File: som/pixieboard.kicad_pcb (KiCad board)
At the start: 8 copper layers, 50 x 50 mm, 11 parts, among them U1 XC7A200T-3FBG484E, U2 AS4C256M16D3, U3 AS4C256M16D3

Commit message: lmfao l
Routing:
- net /DDR3/DDR_D23: track 34.2 -> 0.57 mm, vias 3 -> 1
- net /DDR3/DDR_D17: track 28.9 -> 0.57 mm, vias 3 -> 1
- net /DDR3/DDR_D19: track 28.4 -> 0.57 mm, vias 2 -> 1
- net /DDR3/DDR_DM2: track 28.1 -> 0.57 mm, vias 3 -> 1
- net /DDR3/DDR_D22: track 27.9 -> 0.57 mm, vias 4 -> 1
- net /DDR3/DDR_D21: track 27.3 -> 0.57 mm, vias 3 -> 1
- net /DDR3/DDR_D30: track 26.2 -> 0.57 mm, vias 3 -> 1
- net /DDR3/DDR_D24: track 25.0 -> 0.57 mm, vias 3 -> 1
- net /DDR3/DDR_D16: track 23.8 -> 0.57 mm, vias 3 -> 1
- net /DDR3/DDR_D20: track 23.6 -> 0.57 mm, vias 4 -> 1
- net /DDR3/DDR_DQS3+: track 23.2 -> 0.57 mm, vias 3 -> 1
- net /DDR3/DDR_DQS2-: track 22.8 -> 0.57 mm, vias 2 -> 1
- net /DDR3/DDR_DQS3-: track 22.4 -> 0.57 mm, vias 3 -> 1
- net /DDR3/DDR_D18: track 22.2 -> 0.57 mm, vias 4 -> 1
- net /DDR3/DDR_DM3: track 21.8 -> 0.57 mm, vias 3 -> 1
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
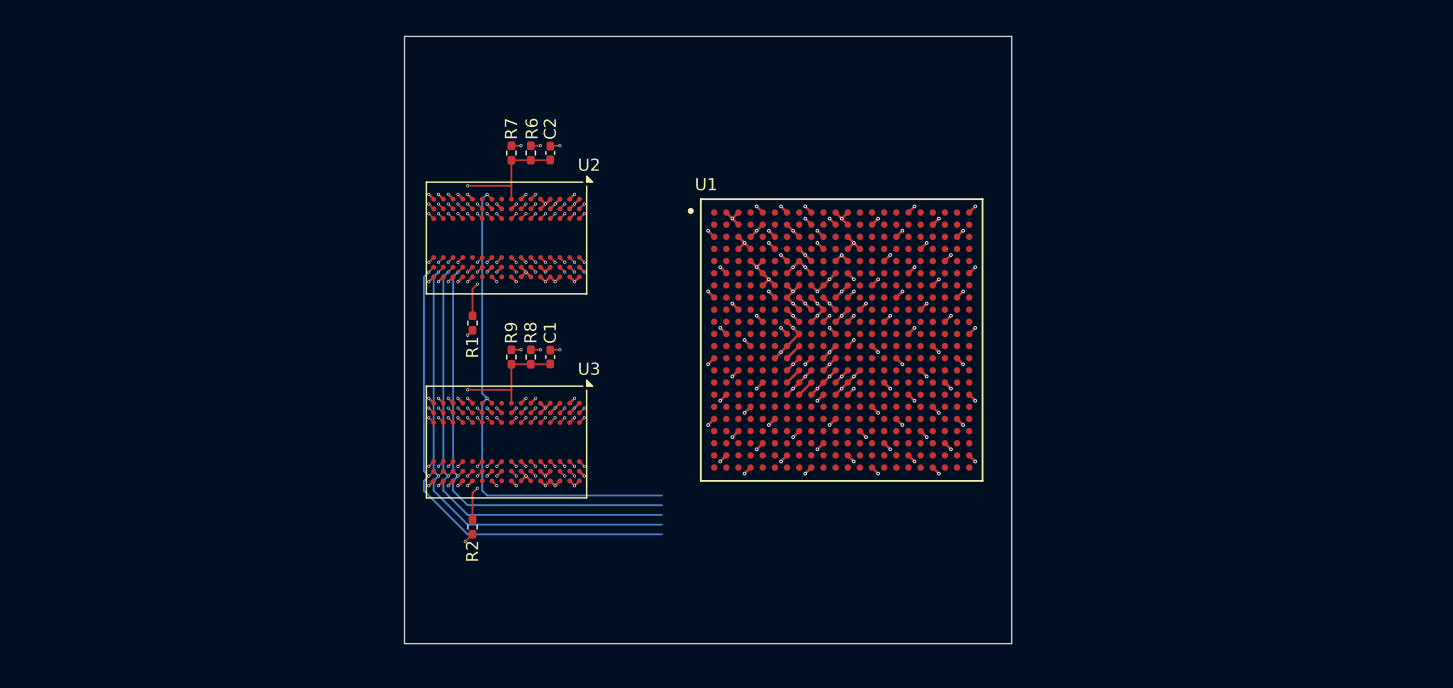
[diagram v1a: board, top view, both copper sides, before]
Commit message: Completed DDR3L routing
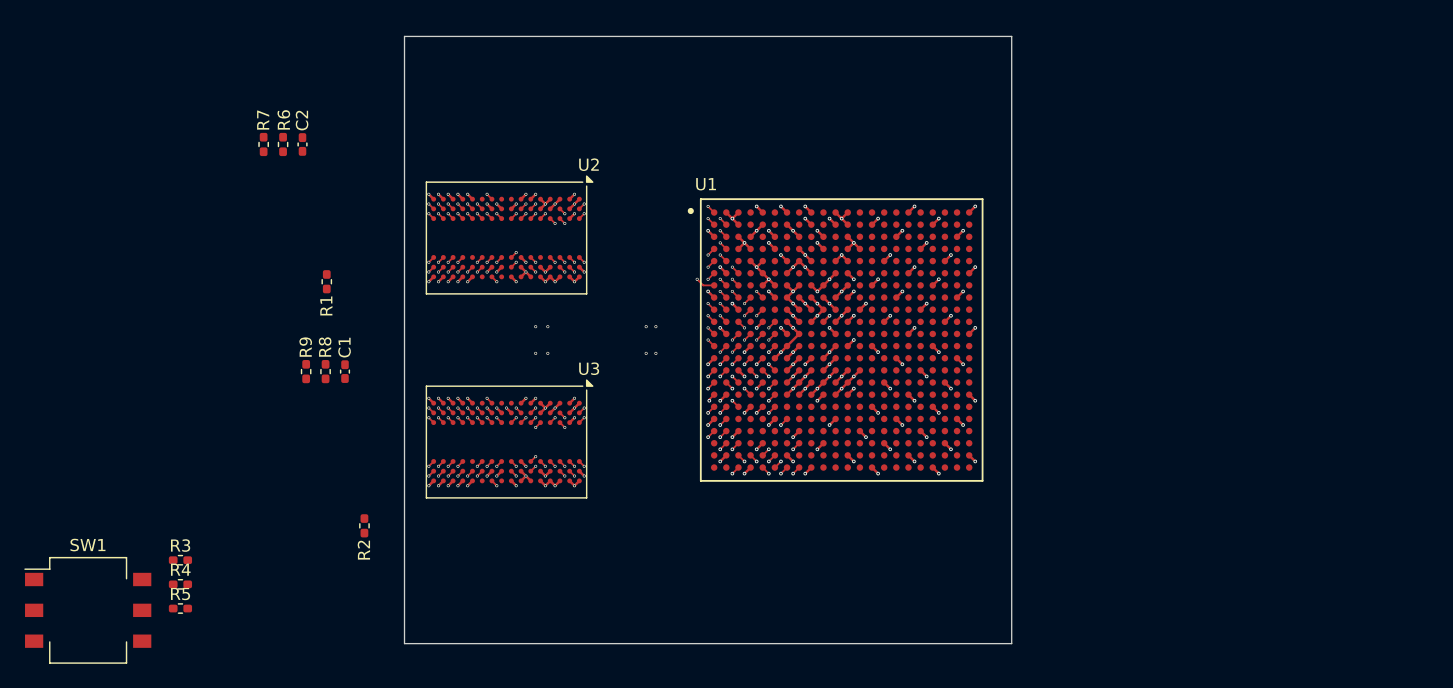
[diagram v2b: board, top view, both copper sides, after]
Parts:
- added R3: 10K, Resistor_SMD:R_0402_1005Metric_Pad0.72x0.64mm_HandSolder, F.Cu at (-54.5, 18.1)
- added R4: 10K, Resistor_SMD:R_0402_1005Metric_Pad0.72x0.64mm_HandSolder, F.Cu at (-54.5, 20.1)
- added R5: 10K, Resistor_SMD:R_0402_1005Metric_Pad0.72x0.64mm_HandSolder, F.Cu at (-54.5, 22.1)
- added SW1: SW_DIP_x03, Button_Switch_SMD:SW_DIP_SPSTx03_Slide_Omron_A6S-310x_W8.9mm_P2.54mm, F.Cu at (-62.0, 22.3)
- moved R7 20.4 mm to (-47.6, -16.1)
- moved C2 20.4 mm to (-44.4, -16.1)
- moved R6 20.4 mm to (-46.0, -16.1)
- moved R9 16.9 mm to (-44.1, 2.60)
- moved C1 16.9 mm to (-40.9, 2.60)
- moved R8 16.9 mm to (-42.5, 2.60)
- moved R1 12.5 mm to (-42.4, -4.80)
- moved R2 8.90 mm to (-39.3, 15.3)
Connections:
- U1 pad A1: /DDR3/DDR_D1 -> /DDR3/DDR_D4
- U1 pad AA1: /DDR3/DDR_A8 -> unconnected-(U1E-IO_L7P_T1_34-PadAA1)
- U1 pad AA3: /DDR3/DDR_A13 -> /DDR3/DDR_BA2
- U1 pad AA4: /DDR3/DDR_BA2 -> /DDR3/DDR_A5
- U1 pad AA5: /DDR3/DDR_A14 -> /DDR3/DDR_A0
- U1 pad AA6: unconnected-(U1E-IO_L18N_T2_34-PadAA6) -> /DDR3/DDR_A7
- U1 pad AA8: /DDR3/~{DDR_RST} -> unconnected-(U1E-IO_L22P_T3_34-PadAA8)
- U1 pad AB1: /DDR3/DDR_A9 -> unconnected-(U1E-IO_L7N_T1_34-PadAB1)
- U1 pad AB2: /DDR3/DDR_A11 -> unconnected-(U1E-IO_L8N_T1_34-PadAB2)
- U1 pad AB3: /DDR3/DDR_A10 -> /DDR3/DDR_A3
- U1 pad AB5: /DDR3/DDR_BA0 -> /DDR3/DDR_A2
- U1 pad AB6: unconnected-(U1E-IO_L20N_T3_34-PadAB6) -> /DDR3/~{DDR_RST}
- U1 pad AB7: unconnected-(U1E-IO_L20P_T3_34-PadAB7) -> /DDR3/DDR_A9
- U1 pad AB8: /DDR3/~{DDR_CS} -> /DDR3/DDR_A13
- U1 pad B1: /DDR3/DDR_D0 -> /DDR3/DDR_D6
- U1 pad B2: /DDR3/DDR_D3 -> /DDR3/DDR_D2
- U1 pad C2: /DDR3/DDR_D2 -> /DDR3/DDR_D0
- U1 pad D2: /DDR3/DDR_D5 -> /DDR3/DDR_D7
- U1 pad E2: /DDR3/DDR_D4 -> /DDR3/DDR_D5
- U1 pad F1: /DDR3/DDR_D7 -> /DDR3/DDR_D3
- U1 pad F3: /DDR3/DDR_DM0 -> /DDR3/DDR_D1
- U1 pad G1: /DDR3/DDR_D6 -> /DDR3/DDR_DM0
- U1 pad G2: /DDR3/DDR_D11 -> /DDR3/DDR_D8
- U1 pad H3: /DDR3/DDR_D12 -> /DDR3/DDR_D15
- U1 pad H4: /DDR3/DDR_DM1 -> /DDR3/DDR_D11
- U1 pad H5: /DDR3/DDR_D15 -> /DDR3/DDR_DM1
- U1 pad J1: /DDR3/DDR_D9 -> /DDR3/DDR_D12
- U1 pad J4: /DDR3/DDR_D17 -> /DDR3/DDR_D22
- U1 pad J5: /DDR3/DDR_D14 -> /DDR3/DDR_D9
- U1 pad J6: /DDR3/DDR_D23 -> unconnected-(U1F-IO_L17N_T2_35-PadJ6)
- U1 pad K1: /DDR3/DDR_D8 -> /DDR3/DDR_D14
- U1 pad K3: /DDR3/DDR_D19 -> /DDR3/DDR_D20
- U1 pad K4: /DDR3/DDR_D16 -> unconnected-(U1F-IO_L13P_T2_MRCC_35-PadK4)
- U1 pad K6: /DDR3/DDR_D22 -> /DDR3/DDR_D18
- U1 pad L3: /DDR3/DDR_D18 -> /DDR3/DDR_D21
- U1 pad L4: unconnected-(U1F-IO_L18N_T2_35-PadL4) -> /DDR3/DDR_D17
- U1 pad L5: /DDR3/DDR_DM2 -> /DDR3/DDR_D19
- U1 pad L6: unconnected-(U1F-IO_25_35-PadL6) -> /DDR3/DDR_D16
- U1 pad M2: /DDR3/DDR_D21 -> /DDR3/DDR_DM2
- U1 pad M3: /DDR3/DDR_D20 -> /DDR3/DDR_D23
- U1 pad M5: /DDR3/DDR_D31 -> unconnected-(U1F-IO_L23N_T3_35-PadM5)
- U1 pad M6: /DDR3/DDR_D30 -> /DDR3/DDR_D25
- U1 pad N2: /DDR3/DDR_D29 -> /DDR3/DDR_D24
- U1 pad N3: /DDR3/DDR_D25 -> /DDR3/DDR_D29
- U1 pad N4: /DDR3/DDR_D24 -> /DDR3/DDR_D31
- U1 pad N5: unconnected-(U1F-IO_L24N_T3_35-PadN5) -> /DDR3/DDR_D27
- U1 pad P1: /DDR3/DDR_D27 -> /DDR3/DDR_D28
- U1 pad P2: /DDR3/DDR_D28 -> /DDR3/DDR_D26
- U1 pad R1: /DDR3/DDR_D26 -> /DDR3/DDR_D30
- U1 pad R2: /DDR3/DDR_A5 -> /DDR3/DDR_CLK-
- U1 pad R3: /DDR3/DDR_A4 -> /DDR3/DDR_CLK+
- U1 pad R6: unconnected-(U1E-IO_L17P_T2_34-PadR6) -> /DDR3/DDR_A12
- U1 pad T1: /DDR3/DDR_A0 -> /DDR3/DDR_CLK_E
- U1 pad T4: unconnected-(U1E-IO_L13N_T2_MRCC_34-PadT4) -> /DDR3/DDR_A10
- U1 pad T6: unconnected-(U1E-IO_L17N_T2_34-PadT6) -> /DDR3/DDR_A1
- U1 pad U1: /DDR3/DDR_A1 -> /DDR3/DDR_ODT
- U1 pad U2: /DDR3/DDR_A2 -> /DDR3/DDR_BA1
- U1 pad U3: unconnected-(U1E-IO_L6P_T0_34-PadU3) -> /DDR3/DDR_A4
- U1 pad U5: unconnected-(U1E-IO_L14N_T2_SRCC_34-PadU5) -> /DDR3/DDR_A6
- U1 pad U6: unconnected-(U1E-IO_L16P_T2_34-PadU6) -> /DDR3/DDR_A8
- U1 pad V2: /DDR3/DDR_A3 -> /DDR3/~{DDR_CS}
- U1 pad V7: /DDR3/DDR_CLK_E -> /DDR3/DDR_A11
- U1 pad W1: unconnected-(U1E-IO_L5P_T0_34-PadW1) -> /DDR3/~{DDR_RAS}
- U1 pad W2: /DDR3/DDR_A6 -> /DDR3/DDR_BA0
- U1 pad W5: /DDR3/DDR_CLK- -> unconnected-(U1E-IO_L15N_T2_DQS_34-PadW5)
- U1 pad W6: /DDR3/DDR_CLK+ -> unconnected-(U1E-IO_L15P_T2_DQS_34-PadW6)
- U1 pad W9: /DDR3/~{DDR_WE} -> unconnected-(U1E-IO_L24P_T3_34-PadW9)
- U1 pad Y2: /DDR3/DDR_A7 -> /DDR3/~{DDR_CAS}
- U1 pad Y3: /DDR3/DDR_A12 -> /DDR3/~{DDR_WE}
- U1 pad Y4: /DDR3/DDR_BA1 -> unconnected-(U1E-IO_L11P_T1_SRCC_34-PadY4)
- U1 pad Y7: /DDR3/~{DDR_CAS} -> unconnected-(U1E-IO_L23N_T3_34-PadY7)
- U1 pad Y8: /DDR3/~{DDR_RAS} -> /DDR3/DDR_A14
- U1 pad Y9: /DDR3/DDR_ODT -> unconnected-(U1E-IO_L24N_T3_34-PadY9)
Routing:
- net /DDR3/DDR_DQS2+: track 0.57 -> 31.6 mm, vias 1 -> 2
- net /DDR3/DDR_DM2: track 0.57 -> 31.6 mm, vias 1 -> 2
- net /DDR3/DDR_DQS2-: track 0.57 -> 31.6 mm, vias 1 -> 2
- net /DDR3/DDR_D23: track 0.57 -> 30.7 mm, vias 1 -> 2
- net /DDR3/DDR_D22: track 0.57 -> 30.7 mm, vias 1 -> 2
- net /DDR3/DDR_D21: track 0.57 -> 30.1 mm, vias 1 -> 2
- net /DDR3/DDR_D20: track 0.57 -> 30.1 mm, vias 1 -> 2
- net /DDR3/DDR_CLK_E: track 32.2 -> 61.6 mm, vias 2 -> 3
- net /DDR3/DDR_D17: track 0.57 -> 29.8 mm, vias 1 -> 2
- net /DDR3/DDR_D18: track 0.57 -> 29.8 mm, vias 1 -> 2
- net /DDR3/DDR_D16: track 0.57 -> 29.2 mm, vias 1 -> 2
- net /DDR3/DDR_D19: track 0.57 -> 29.1 mm, vias 1 -> 2
- net /DDR3/DDR_CLK+: track 34.9 -> 61.5 mm, vias 2 -> 3
- net /DDR3/DDR_DM1: track 0.57 -> 26.6 mm, vias 1 -> 2
- net /DDR3/DDR_DQS1+: track 0.57 -> 26.5 mm, vias 1 -> 2
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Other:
- board text added: "T0"
- board text added: "T1"
- board text added: "T2"
- board text added: "T3"

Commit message: Mezz Power Tweak Ok
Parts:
- added C10: 100nF, Capacitor_SMD:C_0402_1005Metric_Pad0.74x0.62mm_HandSolder, B.Cu at (0.50, 2.50)
- added C11: 100nF, Capacitor_SMD:C_0402_1005Metric_Pad0.74x0.62mm_HandSolder, B.Cu at (0.50, -2.50)
- added C12: 100nF, Capacitor_SMD:C_0402_1005Metric_Pad0.74x0.62mm_HandSolder, B.Cu at (-9.50, -2.00)
- added C13: 100nF, Capacitor_SMD:C_0402_1005Metric_Pad0.74x0.62mm_HandSolder, B.Cu at (-10.0, -9.50)
- added C14: 100nF, Capacitor_SMD:C_0402_1005Metric_Pad0.74x0.62mm_HandSolder, B.Cu at (-9.00, -5.50)
- added C15: 100nF, Capacitor_SMD:C_0402_1005Metric_Pad0.74x0.62mm_HandSolder, B.Cu at (-7.00, 6.50)
- added C16: 100nF, Capacitor_SMD:C_0402_1005Metric_Pad0.74x0.62mm_HandSolder, B.Cu at (-7.50, 3.50)
- added C17: 100nF, Capacitor_SMD:C_0402_1005Metric_Pad0.74x0.62mm_HandSolder, B.Cu at (-7.50, 10.0)
- added C18: 100nF, Capacitor_SMD:C_0402_1005Metric_Pad0.74x0.62mm_HandSolder, B.Cu at (7.00, -10.5)
- added C19: 100nF, Capacitor_SMD:C_0402_1005Metric_Pad0.74x0.62mm_HandSolder, B.Cu at (5.00, -6.50)
- added C20: 100nF, Capacitor_SMD:C_0402_1005Metric_Pad0.74x0.62mm_HandSolder, B.Cu at (10.0, -6.50)
- added C21: 100nF, Capacitor_SMD:C_0402_1005Metric_Pad0.74x0.62mm_HandSolder, B.Cu at (8.00, -2.50)
- added C22: 100nF, Capacitor_SMD:C_0402_1005Metric_Pad0.74x0.62mm_HandSolder, B.Cu at (2.50, -4.00)
- added C23: 100nF, Capacitor_SMD:C_0402_1005Metric_Pad0.74x0.62mm_HandSolder, B.Cu at (9.00, 1.44)
- added C24: 100nF, Capacitor_SMD:C_0402_1005Metric_Pad0.74x0.62mm_HandSolder, B.Cu at (8.00, 8.50)
- added C25: 100nF, Capacitor_SMD:C_0402_1005Metric_Pad0.74x0.62mm_HandSolder, B.Cu at (8.00, 3.50)
- added C26: 100nF, Capacitor_SMD:C_0402_1005Metric_Pad0.74x0.62mm_HandSolder, B.Cu at (5.00, 4.50)
- added C27: 100nF, Capacitor_SMD:C_0402_1005Metric_Pad0.74x0.62mm_HandSolder, B.Cu at (0.50, 4.50)
- added C28: 100nF, Capacitor_SMD:C_0402_1005Metric_Pad0.74x0.62mm_HandSolder, B.Cu at (5.00, 9.50)
- added C29: 100nF, Capacitor_SMD:C_0402_1005Metric_Pad0.74x0.62mm_HandSolder, B.Cu at (-1.50, 8.00)
- added C3: 100nF, Capacitor_SMD:C_0402_1005Metric_Pad0.74x0.62mm_HandSolder, B.Cu at (-1.50, -3.50)
- added C30: 100nF, Capacitor_SMD:C_0402_1005Metric_Pad0.74x0.62mm_HandSolder, B.Cu at (-2.50, -7.50)
- added C31: 100nF, Capacitor_SMD:C_0402_1005Metric_Pad0.74x0.62mm_HandSolder, B.Cu at (-0.50, 0.00)
- added C4: 100nF, Capacitor_SMD:C_0402_1005Metric_Pad0.74x0.62mm_HandSolder, B.Cu at (-3.50, -2.50)
- added C5: 100nF, Capacitor_SMD:C_0402_1005Metric_Pad0.74x0.62mm_HandSolder, B.Cu at (-4.50, 0.50)
- added C6: 100nF, Capacitor_SMD:C_0402_1005Metric_Pad0.74x0.62mm_HandSolder, B.Cu at (-3.50, 4.50)
- added C7: 100nF, Capacitor_SMD:C_0402_1005Metric_Pad0.74x0.62mm_HandSolder, B.Cu at (-1.50, 2.50)
- added C8: 100nF, Capacitor_SMD:C_0402_1005Metric_Pad0.74x0.62mm_HandSolder, B.Cu at (-3.50, 2.50)
- added C9: 100nF, Capacitor_SMD:C_0402_1005Metric_Pad0.74x0.62mm_HandSolder, B.Cu at (-5.50, -7.50)
- added H1: MountingHole_Pad, MountingHole:MountingHole_2.2mm_M2_DIN965_Pad, F.Cu at (11.5, -22.5)
- added H2: MountingHole_Pad, MountingHole:MountingHole_2.2mm_M2_DIN965_Pad, F.Cu at (-33.5, -22.5)
- added H3: MountingHole_Pad, MountingHole:MountingHole_2.2mm_M2_DIN965_Pad, F.Cu at (11.5, 22.5)
- added H4: MountingHole_Pad, MountingHole:MountingHole_2.2mm_M2_DIN965_Pad, F.Cu at (-33.5, 22.5)
- added J1: Conn_02x20_Counter_Clockwise, Mezzanine:Mezz_02x20_p0.5mm_M, B.Cu at (-17.0, -22.5)
- added J2: Conn_02x20_Counter_Clockwise, Mezzanine:Mezz_02x20_p0.5mm_M, B.Cu at (-5.00, -22.5)
- added J3: Conn_02x20_Counter_Clockwise, Mezzanine:Mezz_02x20_p0.5mm_M, B.Cu at (-5.00, 22.5)
- added J4: Conn_02x20_Counter_Clockwise, Mezzanine:Mezz_02x20_p0.5mm_M, B.Cu at (-17.0, 22.5)
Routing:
- net GND: track 103.3 -> 122.2 mm
- net +3V3: track 10.8 -> 16.9 mm, vias 2 -> 3
- net +1V0: track 16.3 -> 21.0 mm
- net +1V35: track 30.0 -> 34.0 mm
- net VBANK16: track 4.24 -> 6.36 mm
- net VBANK15: track 4.24 -> 6.36 mm
- net VBANK14: track 4.24 -> 6.36 mm
- net VBANK13: track 3.54 -> 4.95 mm
- net +1V8: track 4.24 -> 5.24 mm
- net unconnected-(J4-Pin_39-Pad39): track 0.00 -> 0.99 mm, vias 0 -> 1
- net unconnected-(J4-Pin_37-Pad37): track 0.00 -> 0.99 mm, vias 0 -> 1
- net unconnected-(J4-Pin_35-Pad35): track 0.00 -> 0.99 mm, vias 0 -> 1
- net unconnected-(J4-Pin_33-Pad33): track 0.00 -> 0.99 mm, vias 0 -> 1
- net unconnected-(J4-Pin_31-Pad31): track 0.00 -> 0.99 mm, vias 0 -> 1
- net unconnected-(J4-Pin_29-Pad29): track 0.00 -> 0.99 mm, vias 0 -> 1
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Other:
- outline, holes or cut-outs redrawn

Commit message: TMP
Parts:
- added J3: Conn_02x20_Counter_Clockwise, Mezzanine:Mezz_02x20_p0.5mm_M, B.Cu at (11.5, -6.00)
- added J4: Conn_02x20_Counter_Clockwise, Mezzanine:Mezz_02x20_p0.5mm_M, B.Cu at (11.5, 6.00)
- moved C12 37.4 mm to (27.9, -1.90)
- moved C13 37.4 mm to (27.4, -9.40)
- moved C14 37.4 mm to (28.4, -5.40)
- moved C15 37.4 mm to (30.4, 6.60)
- moved C16 37.4 mm to (29.9, 3.60)
- moved C17 37.4 mm to (29.9, 10.1)
- moved C9 37.4 mm to (31.9, -7.40)
- moved C10 37.4 mm to (37.9, 2.60)
- moved C11 37.4 mm to (37.9, -2.40)
- moved C18 37.4 mm to (44.4, -10.4)
- moved C19 37.4 mm to (42.4, -6.40)
- moved C20 37.4 mm to (47.4, -6.40)
- moved C21 37.4 mm to (45.4, -2.40)
- moved C22 37.4 mm to (39.9, -3.90)
- moved C23 37.4 mm to (46.4, 1.54)
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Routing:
- net GND: track 122.2 -> 0.00 mm, vias 103 -> 0
- net /DDR3/DDR_ODT: track 63.0 -> 0.00 mm, vias 3 -> 0
- net /DDR3/DDR_A8: track 62.9 -> 0.00 mm, vias 3 -> 0
- net /DDR3/DDR_A4: track 62.9 -> 0.00 mm, vias 3 -> 0
- net /DDR3/DDR_A6: track 62.9 -> 0.00 mm, vias 3 -> 0
- net /DDR3/DDR_BA1: track 62.9 -> 0.00 mm, vias 3 -> 0
- net /DDR3/~{DDR_RST}: track 62.3 -> 0.00 mm, vias 3 -> 0
- net /DDR3/DDR_A7: track 62.2 -> 0.00 mm, vias 3 -> 0
- net /DDR3/DDR_A13: track 62.2 -> 0.00 mm, vias 3 -> 0
- net /DDR3/~{DDR_CS}: track 62.1 -> 0.00 mm, vias 3 -> 0
- net /DDR3/DDR_A5: track 62.1 -> 0.00 mm, vias 3 -> 0
- net /DDR3/DDR_BA0: track 62.1 -> 0.00 mm, vias 3 -> 0
- net /DDR3/DDR_A9: track 62.1 -> 0.00 mm, vias 3 -> 0
- net /DDR3/DDR_A0: track 62.0 -> 0.00 mm, vias 3 -> 0
- net /DDR3/DDR_A2: track 62.0 -> 0.00 mm, vias 3 -> 0
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- added copper zone on In1.Cu, net GND
- added copper zone on In4.Cu, net GND
- added copper zone on In6.Cu, net GND
- removed copper zone on In2.Cu, net +1V0
- removed copper zone on In2.Cu, net +1V2
- removed copper zone on In2.Cu, net +1V35
- removed copper zone on In2.Cu, net +1V8
- removed copper zone on In2.Cu, net VBANK13
- removed copper zone on In2.Cu, net VBANK14
- removed copper zone on In2.Cu, net VBANK15
- removed copper zone on In2.Cu, net VBANK16
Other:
- board text removed: "Bank 0"
- board text removed: "Bank 13"
- board text removed: "Bank 14"
- board text removed: "Bank 15"
- board text removed: "Bank 16"
- board text removed: "Bank 34"
- board text removed: "Bank 35"
- board text removed: "HS diff"
- board text removed: "T0"
- board text removed: "T1"
- board text removed: "T2"
- board text removed: "T3"
- board text removed: "cfg"

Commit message: lol
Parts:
- moved U2 10.3 mm to (-19.2, -7.60)
- moved U1 9.50 mm to (1.00, 0.00), turned to 0 degrees
- moved U3 9.48 mm to (-19.2, 7.60)
- moved H1 8.50 mm to (20.0, -22.5)
- moved H2 8.50 mm to (-25.0, -22.5)
- moved H3 8.50 mm to (20.0, 22.5)
- moved H4 8.50 mm to (-25.0, 22.5)
- moved J1 8.50 mm to (-8.50, -22.5)
- moved J2 8.50 mm to (3.50, -22.5)
- moved J3 8.50 mm to (3.50, 22.5)
- moved J3 8.50 mm to (20.0, -6.00)
- moved J4 8.50 mm to (-8.50, 22.5)
- moved J4 8.50 mm to (20.0, 6.00)
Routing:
- net /DDR3/DDR_ODT: track 0.00 -> 25.9 mm, vias 0 -> 6
- net /DDR3/DDR_CLK+: track 0.00 -> 25.9 mm, vias 0 -> 5
- net /DDR3/DDR_CLK-: track 0.00 -> 25.9 mm, vias 0 -> 5
- net /DDR3/~{DDR_RST}: track 0.00 -> 25.9 mm, vias 0 -> 4
- net /DDR3/~{DDR_CS}: track 0.00 -> 25.9 mm, vias 0 -> 4
- net /DDR3/DDR_CLK_E: track 0.00 -> 25.9 mm, vias 0 -> 2
- net /DDR3/DDR_A7: track 0.00 -> 25.9 mm, vias 0 -> 3
- net /DDR3/DDR_A8: track 0.00 -> 25.9 mm, vias 0 -> 3
- net /DDR3/DDR_A6: track 0.00 -> 25.9 mm, vias 0 -> 2
- net /DDR3/DDR_A14: track 0.00 -> 25.9 mm, vias 0 -> 5
- net /DDR3/DDR_A11: track 0.00 -> 25.9 mm, vias 0 -> 4
- net /DDR3/DDR_A10: track 0.00 -> 25.9 mm, vias 0 -> 5
- net /DDR3/~{DDR_WE}: track 0.00 -> 25.9 mm, vias 0 -> 1
- net /DDR3/~{DDR_CAS}: track 0.00 -> 25.9 mm, vias 0 -> 1
- net /DDR3/DDR_BA0: track 0.00 -> 25.9 mm, vias 0 -> 3
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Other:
- board text removed: "C"
- board text removed: "D"
- board text removed: "P"
